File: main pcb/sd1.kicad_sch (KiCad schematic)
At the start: 14 parts

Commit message: fixed con2
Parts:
- ARCADE_PCB_CONN1: footprint Connector_Harwin:Harwin_Gecko-G125-FVX1205L0X_2x06_P1.25mm_Vertical -> Connector_PinHeader_2.54mm:PinHeader_2x06_P2.54mm_Vertical
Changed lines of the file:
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@@
 			)
 		)
-		(property "Footprint" "Connector_Harwin:Harwin_Gecko-G125-FVX1205L0X_2x06_P1.25mm_Vertical"
+		(property "Footprint" "Connector_PinHeader_2.54mm:PinHeader_2x06_P2.54mm_Vertical"
 			(at 259.08 124.46 0)
 			(effects

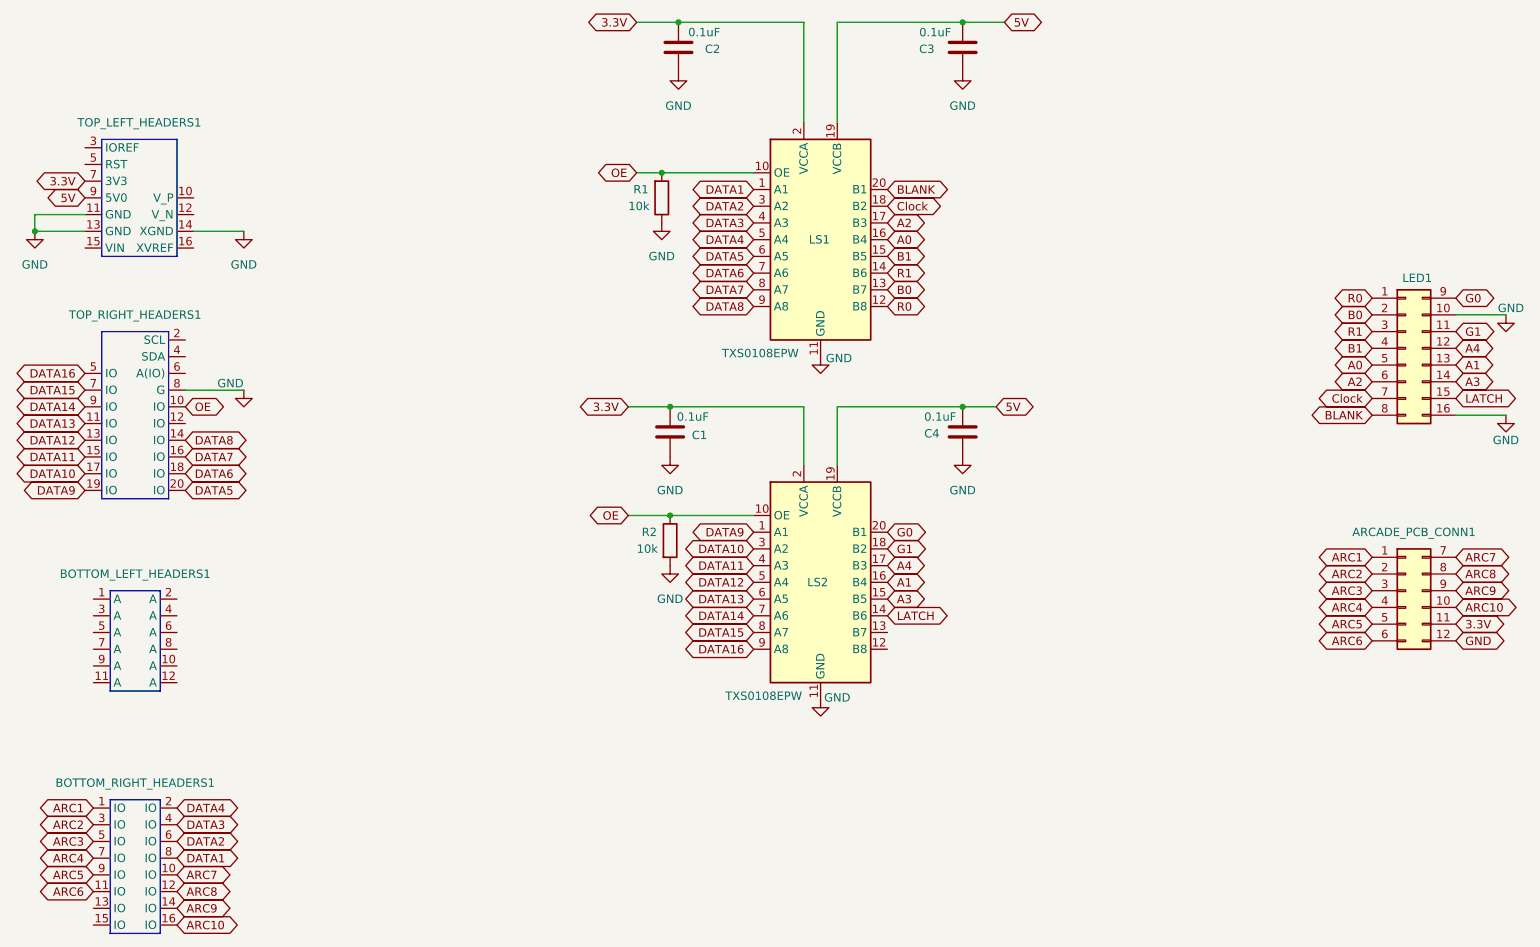
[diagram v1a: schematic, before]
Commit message: wired new connector
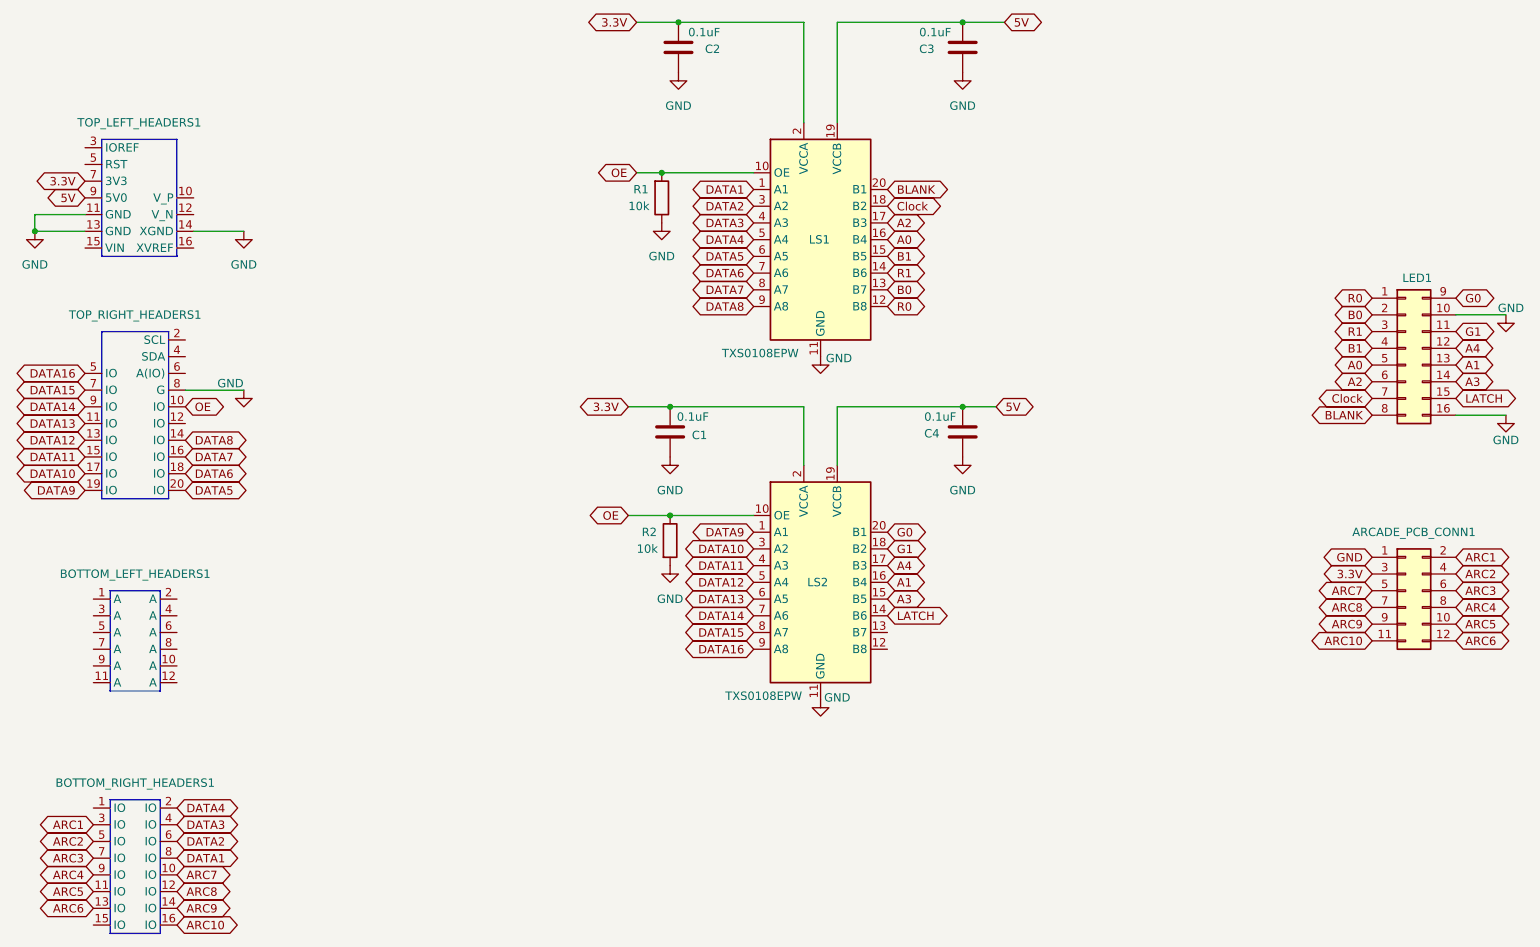
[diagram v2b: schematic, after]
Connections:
- net 3.3V: now also ARCADE_PCB_CONN1.3 (Pin_3); no longer ARCADE_PCB_CONN1.11 (Pin_11)
- net ARC1: now also ARCADE_PCB_CONN1.2 (Pin_2), BOTTOM_RIGHT_HEADERS1.3 (IO); no longer ARCADE_PCB_CONN1.1 (Pin_1), BOTTOM_RIGHT_HEADERS1.1 (IO)
- net ARC10: now also ARCADE_PCB_CONN1.11 (Pin_11); no longer ARCADE_PCB_CONN1.10 (Pin_10)
- net ARC2: now also ARCADE_PCB_CONN1.4 (Pin_4), BOTTOM_RIGHT_HEADERS1.5 (IO); no longer ARCADE_PCB_CONN1.2 (Pin_2), BOTTOM_RIGHT_HEADERS1.3 (IO)
- net ARC3: now also ARCADE_PCB_CONN1.6 (Pin_6), BOTTOM_RIGHT_HEADERS1.7 (IO); no longer ARCADE_PCB_CONN1.3 (Pin_3), BOTTOM_RIGHT_HEADERS1.5 (IO)
- net ARC4: now also ARCADE_PCB_CONN1.8 (Pin_8), BOTTOM_RIGHT_HEADERS1.9 (IO); no longer ARCADE_PCB_CONN1.4 (Pin_4), BOTTOM_RIGHT_HEADERS1.7 (IO)
- net ARC5: now also ARCADE_PCB_CONN1.10 (Pin_10), BOTTOM_RIGHT_HEADERS1.11 (IO); no longer ARCADE_PCB_CONN1.5 (Pin_5), BOTTOM_RIGHT_HEADERS1.9 (IO)
- net ARC6: now also ARCADE_PCB_CONN1.12 (Pin_12), BOTTOM_RIGHT_HEADERS1.13 (IO); no longer ARCADE_PCB_CONN1.6 (Pin_6), BOTTOM_RIGHT_HEADERS1.11 (IO)
- net ARC7: now also ARCADE_PCB_CONN1.5 (Pin_5); no longer ARCADE_PCB_CONN1.7 (Pin_7)
- net ARC8: now also ARCADE_PCB_CONN1.7 (Pin_7); no longer ARCADE_PCB_CONN1.8 (Pin_8)
- net GND: now also ARCADE_PCB_CONN1.1 (Pin_1); no longer ARCADE_PCB_CONN1.12 (Pin_12)
